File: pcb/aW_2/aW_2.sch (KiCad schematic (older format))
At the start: 90 parts

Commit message: Added USB controller and reset button
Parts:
- added C?: 0.1uF, symbol Device:C_Small
- added C? (x2): 47pF, symbol Device:C_Small
- added JP?: SolderJumper_3_Open, symbol Jumper:SolderJumper_3_Open
- added R? (x2): 27, symbol Device:R_Small
- added R? (x2): 1k, symbol Device:R_Small
- added R?: 10k, symbol Device:R_Small
- added SW?: BTN1, symbol Switch:SW_Push
- added SW?: BTN2, symbol Switch:SW_Push
- added U?: FT231XS-R, SOP63P599X175-20N, symbol SnapEDA-Library:FT231XS-R
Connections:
- net +3V3: now also JP?.1 (A), R?.1
- net GND: now also C?.2, C?.2, C?.2, JP?.3 (B), SW?.2, SW?.2, U?.16 (GND), U?.6 (GND)
- net VBUS: now also U?.15 (VCC)
- net main_usb_dn: now also C?.1, R?.2
- net main_usb_dp: now also C?.1, R?.2
- net reset: now also R?.2, SW?.1
- net uart_rx: now also R?.2, U?.20 (TXD); no longer U?.17 (SIO_08/UART_RX)
- net uart_tx: now also R?.2, U?.4 (RXD); no longer U?.19 (SIO_06/UART_TX)
- net uart_cts: now reaches U?.18 (SIO_07/UART_CTS)
- net uart_cts: now also U?.2 (~RTS~)
- net uart_rts: now reaches U?.20 (SIO_05/UART_RTS/AIN3)
- net uart_rts: now also U?.9 (~CTS~)
- net btn2: now reaches U?.21 (SIO_04/AIN2)
- net btn2: now also SW?.1
- net at U?.28 (SIO_13/NAUTORUN): now also JP?.2 (C)
- new net: R?.1, U?.11 (USBDP)
- new net: R?.1, U?.12 (USBDM)
- new net: C?.1, U?.13 (3V3OUT), U?.14 (~RESET~), U?.3 (VCCIO)
- new net: R?.1, U?.17 (SIO_08/UART_RX)
- new net: R?.1, U?.19 (SIO_06/UART_TX)
- new net dtr: U?.1 (~DTR~)

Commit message: Added additional leds and buttons, decoupling capacitors, component mappings
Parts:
- removed Q?: Q_PMOS_DGS, symbol Device:Q_PMOS_DGS
- added BT1: Battery_Cell, Connector_JST:JST_PH_S2B-PH-SM4-TB_1x02-1MP_P2.00mm_Horizontal, symbol Device:Battery_Cell
- added C1, C7: 0.1uF, Capacitor_SMD:C_0402_1005Metric, symbol Device:C_Small
- added C4, C8: 4.7uF, Capacitor_SMD:C_0402_1005Metric, symbol Device:C_Small
- added D2: Orange, LED_SMD:LED_0805_2012Metric, symbol Device:LED_Small
- added D36: Blue, LED_SMD:LED_0805_2012Metric, symbol Device:LED
- added Q1: Q_PMOS_SDG, snap-eda:SOT23, symbol Device:Q_PMOS_SDG
- added R1: 10k, Resistor_SMD:R_0402_1005Metric, symbol Device:R_Small
- added R15, R7: 1k, Resistor_SMD:R_0402_1005Metric, symbol Device:R_Small
- C10, C12, C13, C6, C9: renamed from C?; footprint (none) -> Capacitor_SMD:C_0402_1005Metric
- C11, C2, C3: renamed from C?; value 10mF -> 10uF; footprint (none) -> Capacitor_SMD:C_0603_1608Metric
- C5: renamed from C?; value 10mF -> 4.7uF; footprint (none) -> Capacitor_SMD:C_0402_1005Metric
- D1: renamed from D?; footprint (none) -> Diode_SMD:D_SOD-123
- J1, J2, J3: renamed from J?; footprint GCT_USB4110-GF-A -> snap-eda:GCT_USB4110-GF-A
- J4: renamed from J?; footprint (none) -> Connector_PinHeader_1.27mm:PinHeader_2x05_P1.27mm_Horizontal
- JP1: renamed from JP?; footprint (none) -> Jumper:SolderJumper-3_P1.3mm_Open_RoundedPad1.0x1.5mm
- K1: renamed from K??; footprint (none) -> keebs:Mx_Alps_150
- K10, K11, K12, K13, K16, K17, K18, K19, K2, K20, K23, K24, K25, K26, K27, K28, K29, K3, K30, K31, K32, K4, K5, K6, K7, K9: renamed from K?; footprint (none) -> keebs:Mx_Alps_100
- K14, K15, K21, K22, K8: renamed from K?; footprint (none) -> keebs:Mx_Alps_150
- K33: renamed from K?; footprint (none) -> keebs:Mx_Alps_200
- R10, R11, R12, R13, R14, R2, R3, R4, R5, R8, R9: renamed from R?; footprint (none) -> Resistor_SMD:R_0402_1005Metric
- R6: renamed from R?; value 10k -> 2.4k; footprint (none) -> Resistor_SMD:R_0402_1005Metric
- U1: renamed from U?; footprint SOT95P285X140-5N -> snap-eda:SOT95P285X140-5N
- U2: renamed from U?; footprint SOP65P780X200-28N -> snap-eda:SOP65P780X200-28N
- U4: renamed from U?; footprint SOP63P599X175-20N -> snap-eda:SOP63P599X175-20N
- U5: renamed from U?; footprint XCVR_BL652-SA-01-T/R -> snap-eda:XCVR_BL652-SA-01-T
- gave numbers to parts that had none: 37
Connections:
- net +3V3: now also C1.1, R1.1; no longer U2.18 (~RESET~)
- net +BATT: now also BT1.1 (+), Q1.1 (S)
- net GND: now also BT1.2 (-), C1.2, C4.2, C7.2, C8.2, D36.1 (K)
- net VBUS: now also C4.1, C7.1, C8.1, D2.2 (A), Q1.3 (G)
- net col3: now also D13.1 (K), D20.1 (K), D27.1 (K)
- net row0: now also K1.2
- net at C3.1, D1.1 (K), R3.1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: now also Q1.2 (D)
- net at U3.1 (STAT): now also R7.1
- net led1: now reaches U5.4 (SIO_22)
- net led1: now also R15.2
- net dtr: no longer names the net of U4.1 (~DTR~)
- new net: R1.2, U2.18 (~RESET~)
- new net: D2.1 (K), R7.2
- new net: D36.2 (A), R15.1
- no-connect marks 0 -> 32
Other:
- moved on the sheet: C5, R12, R13, R6, U2, U3

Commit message: Finished keyboard matrix wiring, left side wiring
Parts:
- BT1: footprint Connector_JST:JST_PH_S2B-PH-SM4-TB_1x02-1MP_P2.00mm_Horizontal -> snap-eda:JST_S2B-PH-SM4-TB(LF)(SN)
- D10, D11, D12, D13, D14, D15, D16, D17, D18, D19, D20, D21, D22, D23, D24, D25, D26, D27, D28, D29, D3, D30, D31, D32, D33, D34, D35, D4, D5, D6, D7, D8, D9: footprint Diode_SMD:D_SOD-123 -> keebs:D_SOD-123_mirrored
- SW1, SW2: footprint (none) -> snap-eda:SW_KMR221GLFS
- Y1: footprint (none) -> snap-eda:XTAL_ECS-.327-12.5-34B-TR
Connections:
- net col0: now also U2.27 (GPA6); no longer U2.21 (GPA0)
- net col1: now also U2.26 (GPA5); no longer U2.22 (GPA1)
- net col2: now also U2.25 (GPA4); no longer U2.23 (GPA2)
- net col4: now also U2.23 (GPA2); no longer U2.25 (GPA4)
- net col5: now also U2.22 (GPA1); no longer U2.26 (GPA5)
- net col6: now also U2.21 (GPA0); no longer U2.27 (GPA6)
- net row0: now also U5.10 (SIO_16/SFLASH_CLK); no longer U5.13 (SIO_11)
- net row1: now also U5.11 (SIO_14/SFLASH_MISO); no longer U5.12 (SIO_12/SFLASH_CS)
- net row2: now also U5.12 (SIO_12/SFLASH_CS); no longer U5.11 (SIO_14/SFLASH_MISO)
- net row3: now also U5.13 (SIO_11); no longer U5.10 (SIO_16/SFLASH_CLK)
- net row4: now also U5.14 (NFC2/SIO_10); no longer U5.8 (SIO_20/SFLASH_MOSI)

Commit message: Traces and pours finished
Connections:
- net +3V3: no longer C1.1, J1.A4/B9 (VBUS), J1.B4/A9 (VBUS), R1.1, U2.9 (VDD)
- new net VDC: C1.1, J1.A4/B9 (VBUS), J1.B4/A9 (VBUS), R1.1, U2.9 (VDD)
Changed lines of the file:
@@
 Wire Wire Line
 	1800 8050 1900 8050
-$Comp
-L Connector:Conn_ARM_JTAG_SWD_10 J4
-U 1 1 5F0E3D13
-P 1500 5700
-F 0 "J4" H 1057 5746 50  0000 R CNN
-F 1 "Conn_ARM_JTAG_SWD_10" V 900 6150 50  0000 R CNN
-F 2 "Connector_PinHeader_1.27mm:PinHeader_2x05_P1.27mm_Horizontal" H 1500 5700 50  0001 C CNN
-F 3 "http://infocenter.arm.com/help/topic/com.arm.doc.ddi0314h/DDI0314H_coresight_components_trm.pdf" V 1150 4450 50  0001 C CNN
-	1    1500 5700
-	1    0    0    -1
-$EndComp
 Text Label 2100 5400 0    50   ~ 0
 reset
@@
 	15500 1800 15600 1800
 $Comp
-L power:+3.3V #PWR06
-U 1 1 5F8347A7
-P 15800 900
-F 0 "#PWR06" H 15800 750 50  0001 C CNN
-F 1 "+3.3V" H 15815 1073 50  0000 C CNN
-F 2 "" H 15800 900 50  0001 C CNN
-F 3 "" H 15800 900 50  0001 C CNN
-	1    15800 900
-	1    0    0    -1
-$EndComp
-$Comp
-L power:+3.3V #PWR05
-U 1 1 5F835952
-P 12950 900
-F 0 "#PWR05" H 12950 750 50  0001 C CNN
-F 1 "+3.3V" H 12965 1073 50  0000 C CNN
-F 2 "" H 12950 900 50  0001 C CNN
-F 3 "" H 12950 900 50  0001 C CNN
-	1    12950 900
-	1    0    0    -1
-$EndComp
-$Comp
 L power:GND #PWR011
 U 1 1 5F836A94
@@
 F 3 "" H 15600 2900 50  0001 C CNN
 	1    15600 2900
-	1    0    0    -1
-$EndComp
-$Comp
-L power:+3.3V #PWR01
-U 1 1 5F83F6AA
-P 13550 850
-F 0 "#PWR01" H 13550 700 50  0001 C CNN
-F 1 "+3.3V" H 13565 1023 50  0000 C CNN
-F 2 "" H 13550 850 50  0001 C CNN
-F 3 "" H 13550 850 50  0001 C CNN
-	1    13550 850
 	1    0    0    -1
 $EndComp
@@
 NoConn ~ 4050 6200
 NoConn ~ 4050 6300
-NoConn ~ 2000 5900
 NoConn ~ 4750 1500
 NoConn ~ 4750 1800
@@
 	2050 9550 2150 9550
 NoConn ~ 4550 8950
+$Comp
+L Connector:Conn_ARM_JTAG_SWD_10 J4
+U 1 1 5F0E3D13
+P 1500 5700
+F 0 "J4" H 1057 5746 50  0000 R CNN
+F 1 "Conn_ARM_JTAG_SWD_10" V 900 6150 50  0000 R CNN
+F 2 "Connector_PinHeader_1.27mm:PinHeader_2x05_P1.27mm_Horizontal" H 1500 5700 50  0001 C CNN
+F 3 "http://infocenter.arm.com/help/topic/com.arm.doc.ddi0314h/DDI0314H_coresight_components_trm.pdf" V 1150 4450 50  0001 C CNN
+	1    1500 5700
+	1    0    0    -1
+$EndComp
+NoConn ~ 2000 5900
+$Comp
+L power:VDC #PWR?
+U 1 1 5EFAF23C
+P 12950 900
+F 0 "#PWR?" H 12950 800 50  0001 C CNN
+F 1 "VDC" H 12965 1073 50  0000 C CNN
+F 2 "" H 12950 900 50  0001 C CNN
+F 3 "" H 12950 900 50  0001 C CNN
+	1    12950 900
+	1    0    0    -1
+$EndComp
+$Comp
+L power:VDC #PWR?
+U 1 1 5EFB03DB
+P 13550 850
+F 0 "#PWR?" H 13550 750 50  0001 C CNN
+F 1 "VDC" H 13565 1023 50  0000 C CNN
+F 2 "" H 13550 850 50  0001 C CNN
+F 3 "" H 13550 850 50  0001 C CNN
+	1    13550 850
+	1    0    0    -1
+$EndComp
+$Comp
+L power:VDC #PWR?
+U 1 1 5EFB1743
+P 15800 900
+F 0 "#PWR?" H 15800 800 50  0001 C CNN
+F 1 "VDC" H 15815 1073 50  0000 C CNN
+F 2 "" H 15800 900 50  0001 C CNN
+F 3 "" H 15800 900 50  0001 C CNN
+	1    15800 900
+	1    0    0    -1
+$EndComp
 $EndSCHEMATC

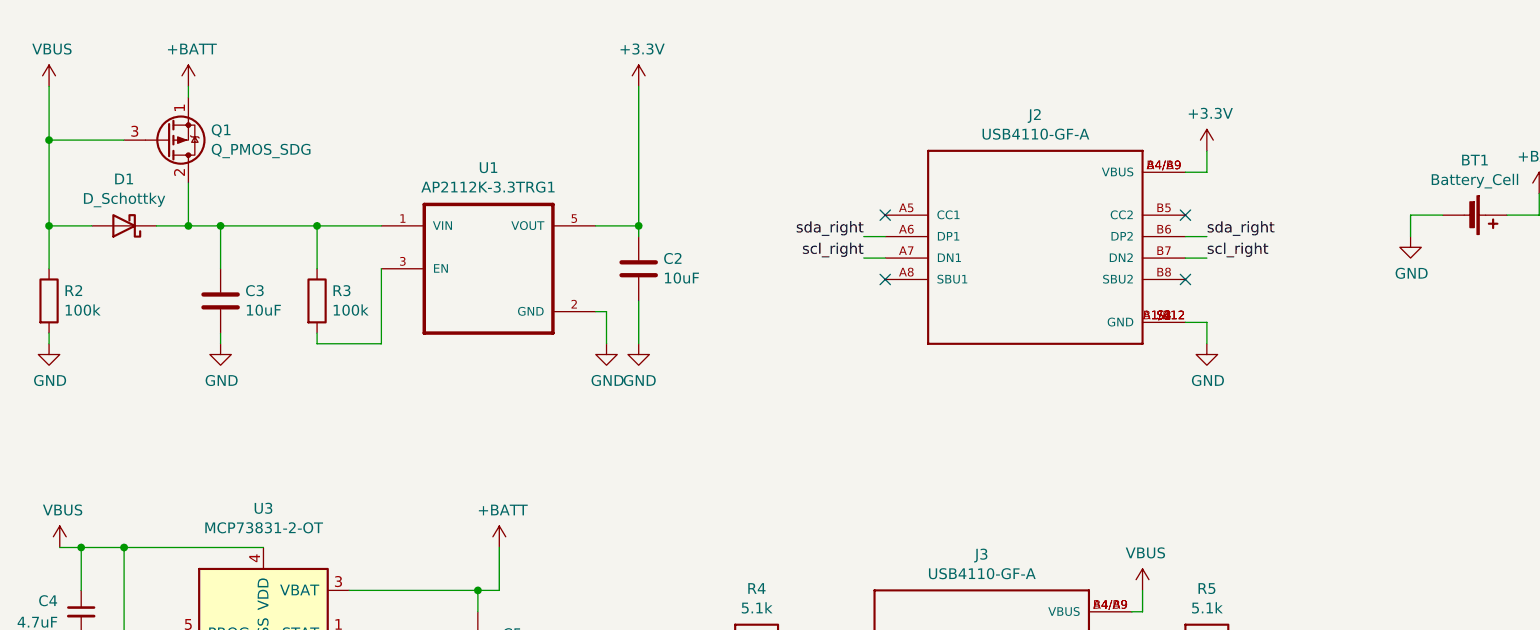
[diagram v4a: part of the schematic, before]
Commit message: Added gerbers, license information, updated connector information
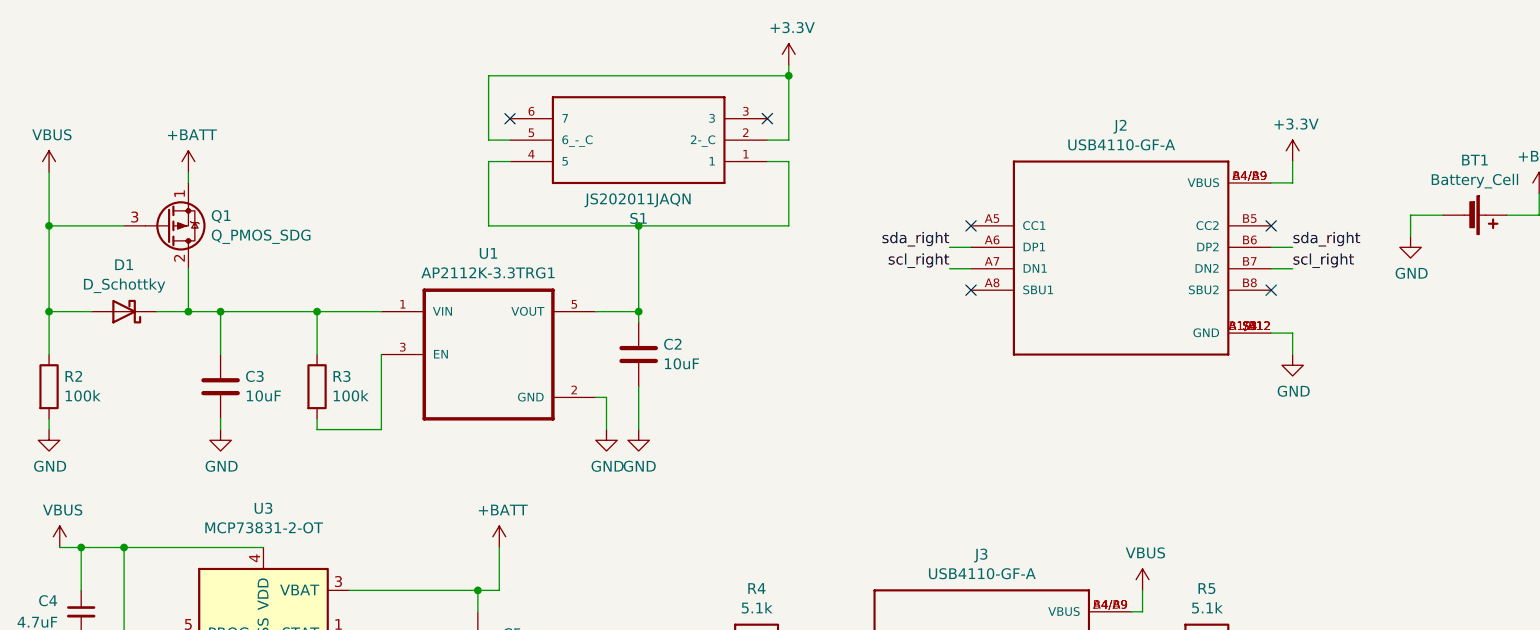
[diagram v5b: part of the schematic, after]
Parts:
- added S1: JS202011JAQN, snap-eda:JS202011JAQN, symbol SnapEDA-Library:JS202011JAQN
- J4: footprint Connector_PinHeader_1.27mm:PinHeader_2x05_P1.27mm_Horizontal -> Connector_PinHeader_1.27mm:PinHeader_2x05_P1.27mm_Vertical
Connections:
- net +3V3: now also S1.2 (2-_C), S1.5 (6_-_C); no longer C2.1, U1.5 (VOUT)
- new net: C2.1, S1.1, S1.4 (5), U1.5 (VOUT)
- no-connect marks 32 -> 34
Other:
- moved on the sheet: C2, C3, D1, J2, Q1, R2, R3, U1
